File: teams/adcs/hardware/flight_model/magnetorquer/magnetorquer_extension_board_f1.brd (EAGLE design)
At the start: 94 x 94 mm, 2 parts

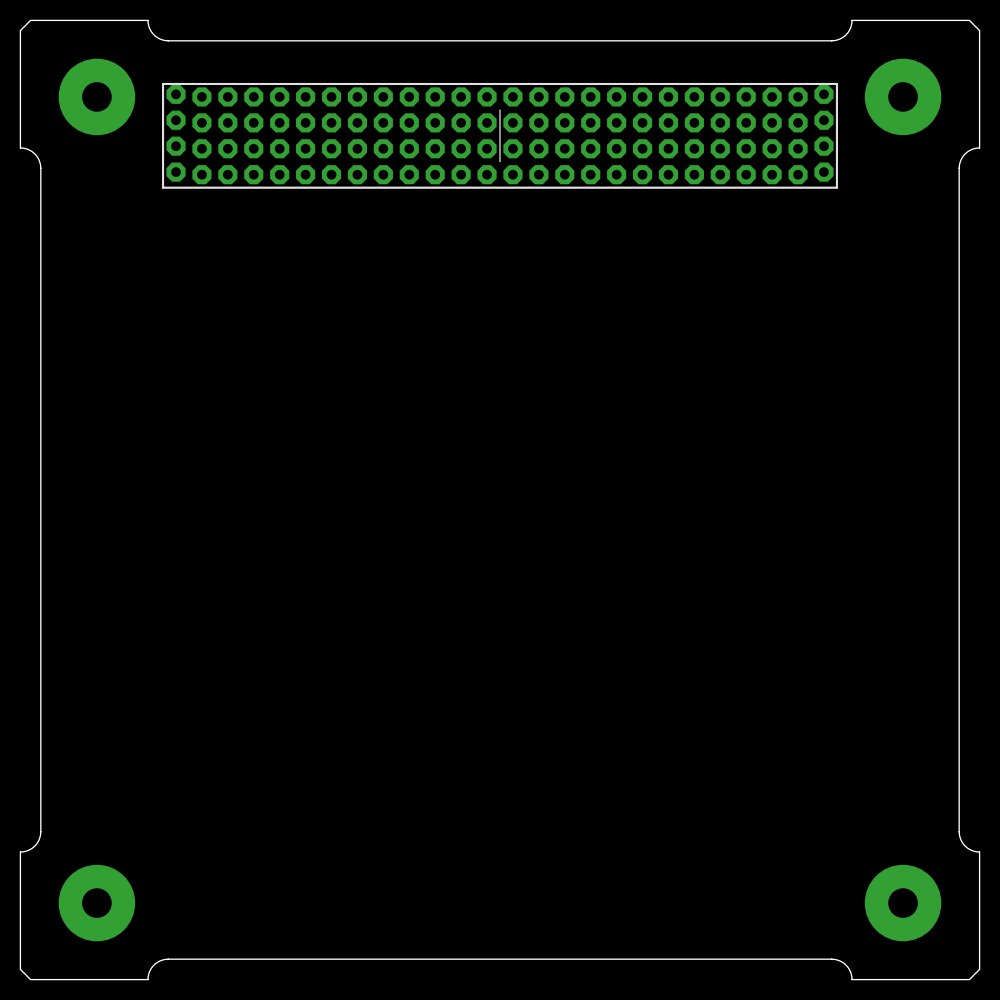
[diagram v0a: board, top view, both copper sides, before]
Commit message: ADCS/MT: Complete magnetorquer extension board
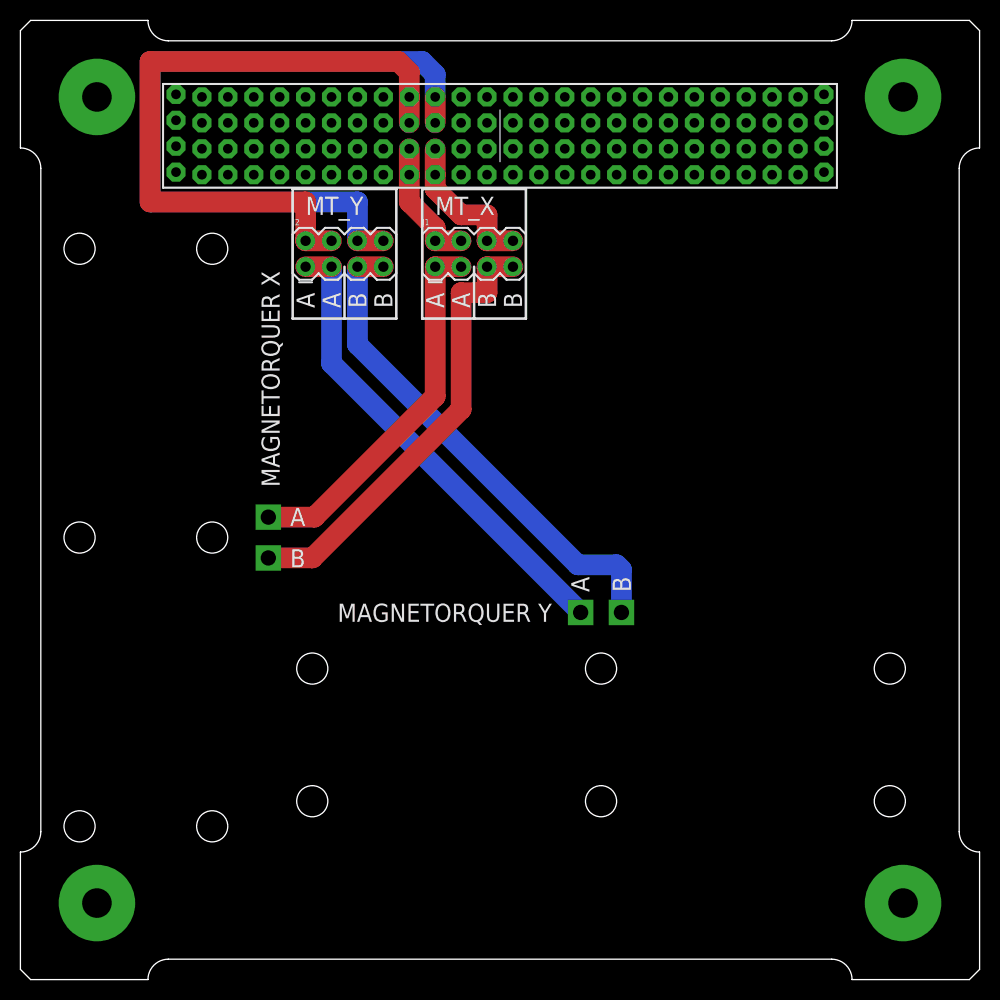
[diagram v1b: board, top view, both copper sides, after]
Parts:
- added J1, J2: (no value), SparkFun-Connectors:2X4
- added MT_X, MT_Y: MT_AIRCORE_HORIZONTAL, DubSat1 Components:MT_AIRCORE_HORIZONTAL
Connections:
- new net MT_X_A: J1.1, J1.3, MT_X.A
- new net MT_X_A_STACK: J1.2, J1.4, U$1.P$37, U$1.P$38
- new net MT_X_B: J1.5, J1.7, MT_X.B
- new net MT_X_B_STACK: J1.6, J1.8, U$1.P$41, U$1.P$42
- new net MT_Y_A: J2.1, J2.3, MT_Y.A
- new net MT_Y_A_STACK: J2.2, J2.4, U$1.P$39, U$1.P$40
- new net MT_Y_B: J2.5, J2.7, MT_Y.B
- new net MT_Y_B_STACK: J2.6, J2.8, U$1.P$43, U$1.P$44
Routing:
- net MT_Y_B_STACK: track 0.00 -> 73.6 mm
- net MT_Y_A_STACK: track 0.00 -> 66.1 mm
- net MT_Y_B: track 0.00 -> 49.4 mm
- net MT_Y_A: track 0.00 -> 46.5 mm
- net MT_X_B: track 0.00 -> 44.0 mm
- net MT_X_A: track 0.00 -> 36.5 mm
- net MT_X_B_STACK: track 0.00 -> 15.2 mm
- net MT_X_A_STACK: track 0.00 -> 12.6 mm
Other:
- board text added: "A"
- board text added: "B"
- board text added: "MAGNETORQUER X"
- board text added: "MAGNETORQUER Y"
- board text added: "MT_X"
- board text added: "MT_Y"
